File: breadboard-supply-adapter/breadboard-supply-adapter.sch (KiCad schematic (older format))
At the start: 8 parts, among them J1 Conn_01x02, J2 Conn_01x02, J3 EURORACK_CONN_16_GATE_CV, J4 Conn_01x04

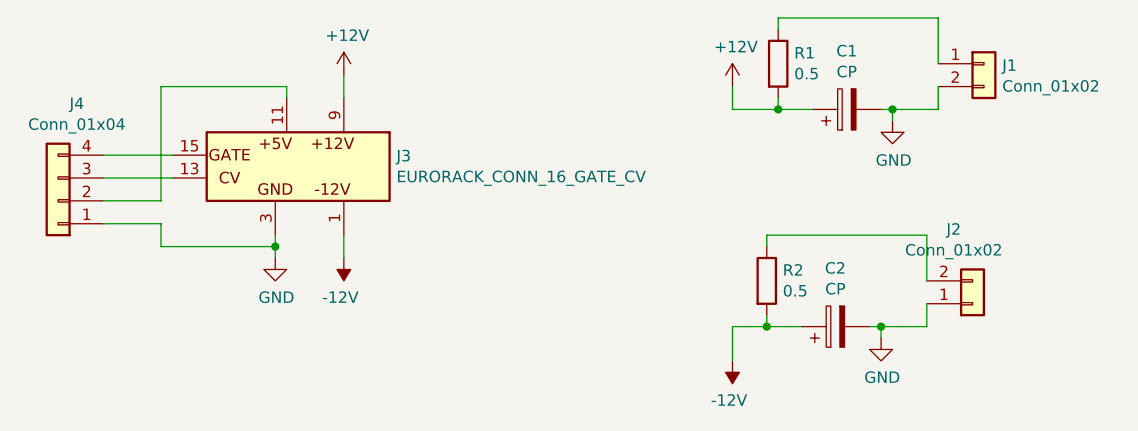
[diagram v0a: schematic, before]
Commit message: reversed the polarity of the neg cap (oops)
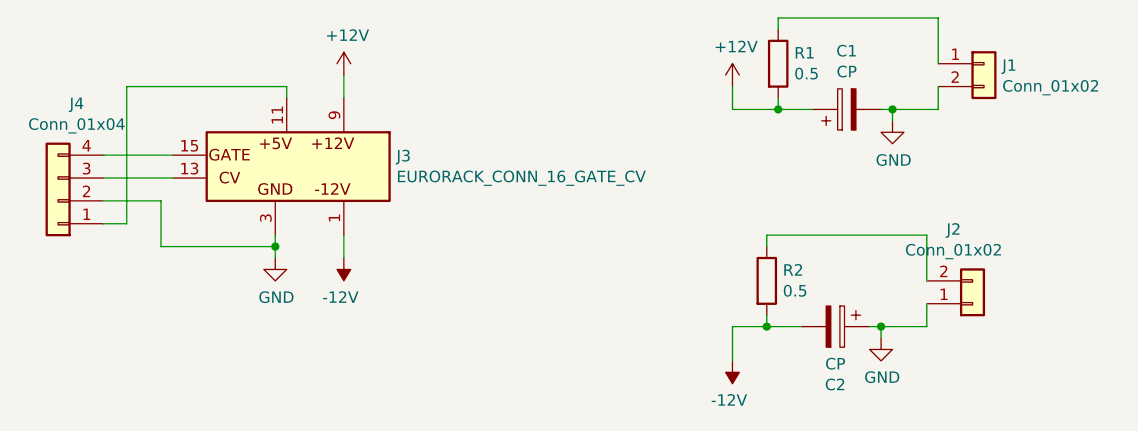
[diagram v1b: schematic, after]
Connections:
- net -12V: now also C2.2; no longer C2.1
- net GND: now also C2.1, J4.2 (Pin_2); no longer C2.2, J4.1 (Pin_1)
- net at J3.11 (5V): now also J4.1 (Pin_1); no longer J4.2 (Pin_2)
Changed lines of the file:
@@
 	3950 2800 3950 2750
 Wire Wire Line
-	3950 2750 3400 2750
-Wire Wire Line
-	3400 2750 3400 3250
-Wire Wire Line
-	3400 3250 3150 3250
-Wire Wire Line
 	3900 3400 3900 3450
-Wire Wire Line
-	3150 3350 3400 3350
-Wire Wire Line
-	3400 3350 3400 3450
 Wire Wire Line
 	3400 3450 3900 3450
@@
 F 3 "~" H 6350 3800 50  0001 C CNN
 	1    6350 3800
-	0    -1   -1   0
+	0    1    1    0
 $EndComp
 $Comp
@@
 	0    -1   -1   0
 $EndComp
+Wire Wire Line
+	3400 3250 3150 3250
+Wire Wire Line
+	3400 3250 3400 3450
+Wire Wire Line
+	3250 2750 3250 3350
+Wire Wire Line
+	3250 3350 3150 3350
+Wire Wire Line
+	3250 2750 3950 2750
 $EndSCHEMATC
